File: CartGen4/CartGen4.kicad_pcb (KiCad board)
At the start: 4 copper layers, 52.8 x 60.9 mm, 81 parts, among them J1 MEM2080-00-128-00-A, J2 Conn_01x05_Male, J3 Conn_02x10_Odd_Even, SW1 EVQ-P7A01P, U1 TPS65266-1RHBR, U10 IS25WP080D-JNLE, U11 DS1391U-33+, U2 SN74LV1T34DCKR, U3 SIT8008BI-73-33E-33.333333G, U4 NXS0108BQX, U5 AS1C8M16PL-70BIN, U6 NXS0108BQX, U7 NXS0108BQX, U8 NXS0104BQX, U9 LFXP2-8E-5MN132C, Y1 FC-135R 32.7680KA-E5

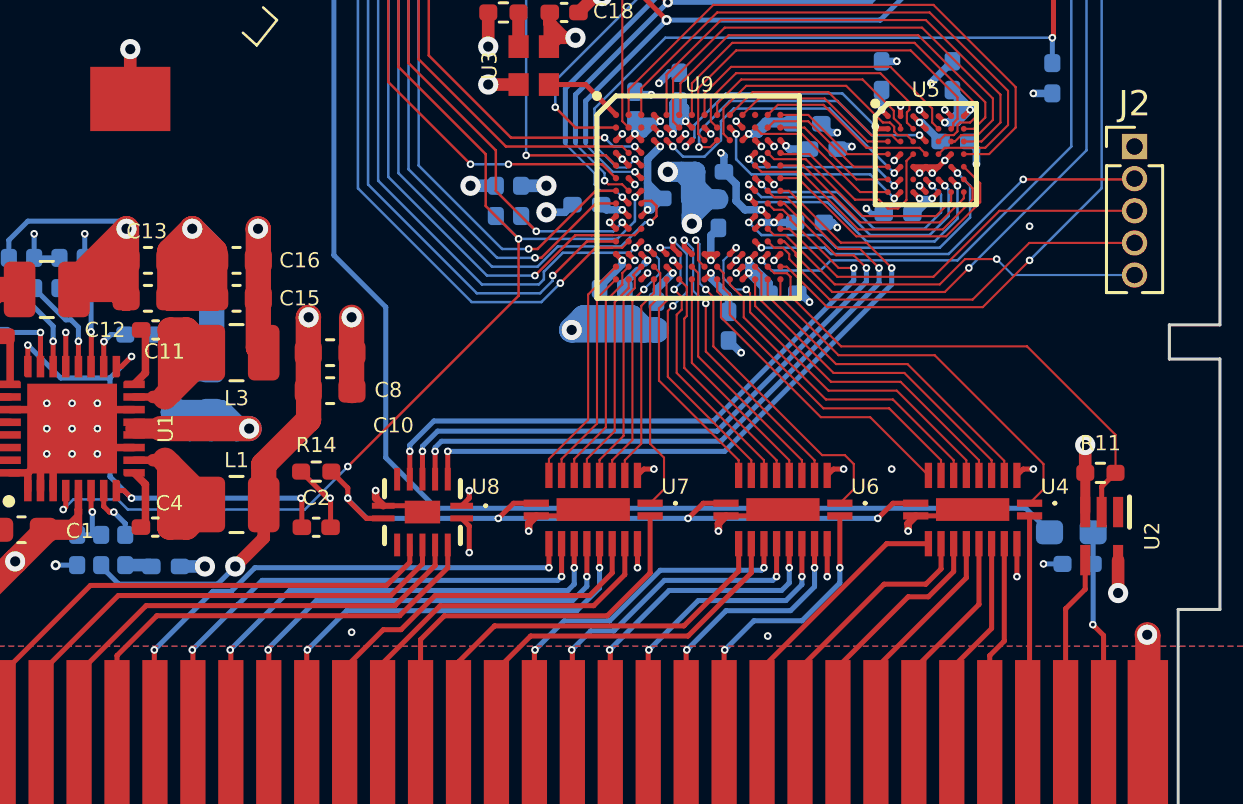
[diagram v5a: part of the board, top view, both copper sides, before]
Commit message: Added bypass capacitors to transceivers
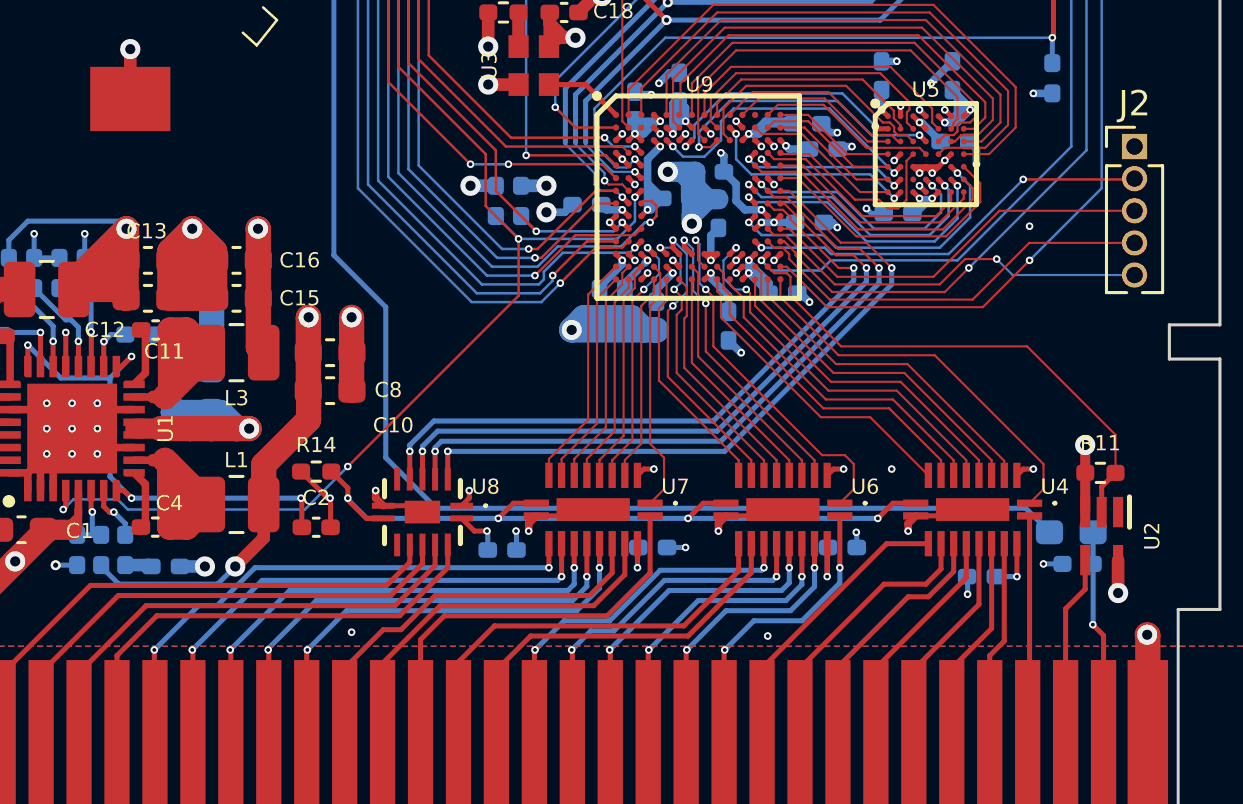
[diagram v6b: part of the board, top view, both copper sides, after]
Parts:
- added C41: 100n, Capacitor_SMD:C_0402_1005Metric_Pad0.74x0.62mm_HandSolder, B.Cu at (64.0, 87.6)
- added C42: 100n, Capacitor_SMD:C_0402_1005Metric_Pad0.74x0.62mm_HandSolder, B.Cu at (70.0, 87.5)
- added C43: 100n, Capacitor_SMD:C_0402_1005Metric_Pad0.74x0.62mm_HandSolder, B.Cu at (77.5, 87.5)
- added C44: 100n, Capacitor_SMD:C_0402_1005Metric_Pad0.74x0.62mm_HandSolder, B.Cu at (83.0, 88.7)
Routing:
- net +5V: track 33.1 -> 36.4 mm
- net GND: track 135.8 -> 138.5 mm, vias 83 -> 87
- net FPGA_USER5: track 42.9 -> 42.2 mm

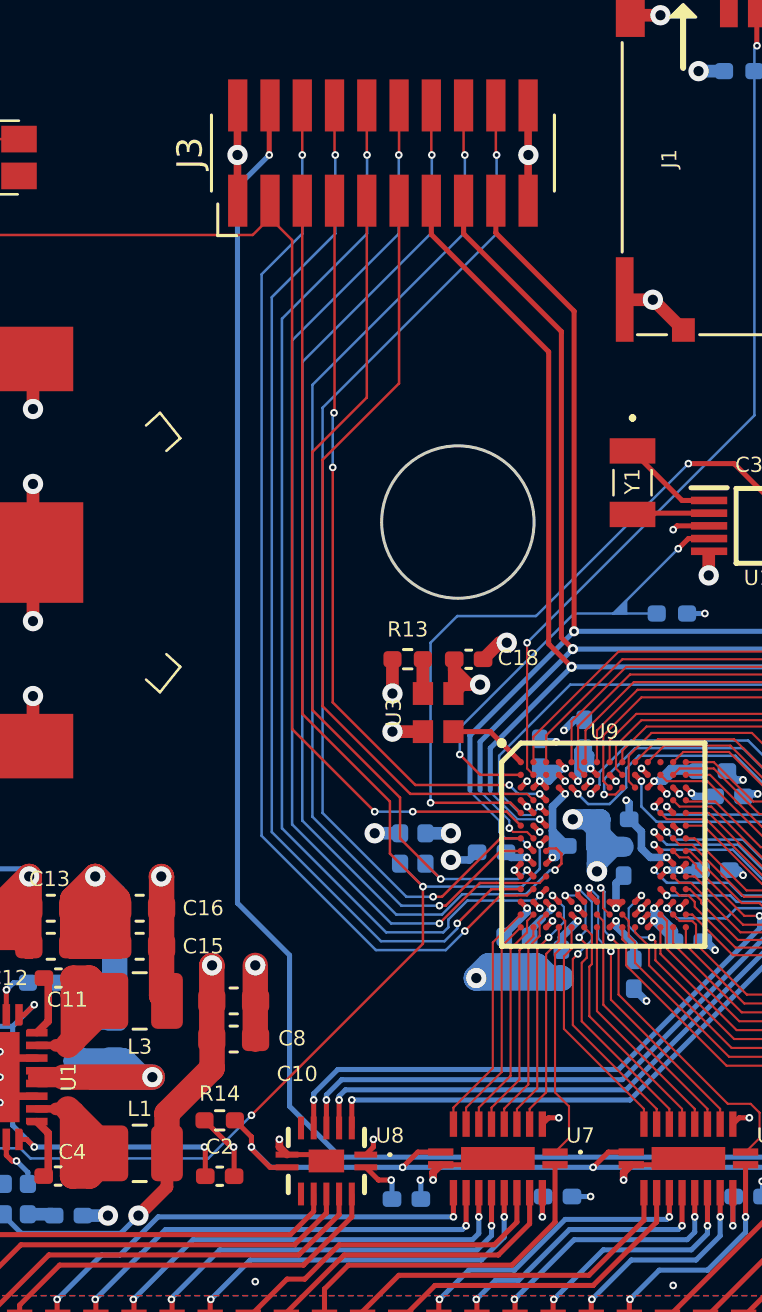
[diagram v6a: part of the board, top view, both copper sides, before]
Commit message: Routed almost forgotten GB_BUS_EN
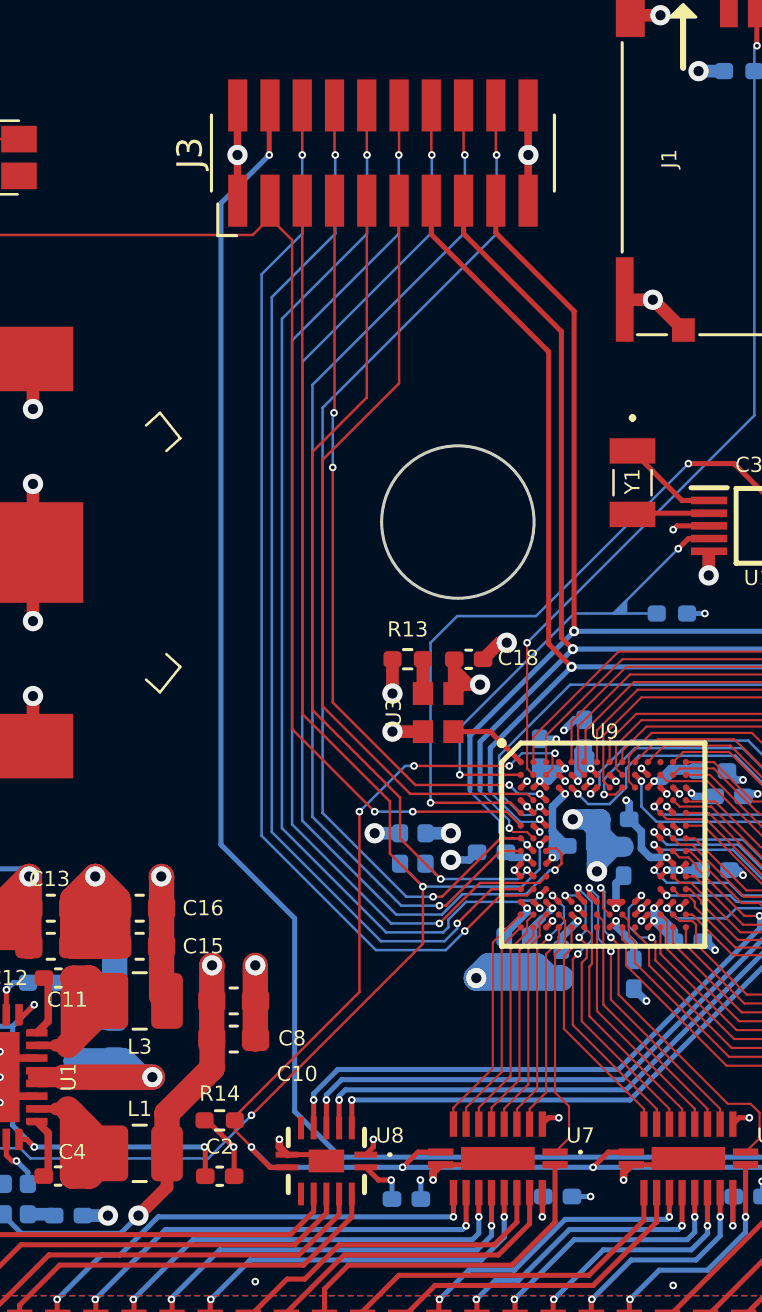
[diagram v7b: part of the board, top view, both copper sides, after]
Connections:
- U9 pad B3: unconnected-(U9-PadB3) -> GB_BUS_EN
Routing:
- net GB_BUS_EN: track 29.6 -> 53.4 mm, vias 4 -> 8
- net GB_AUDIO: track 68.2 -> 68.8 mm

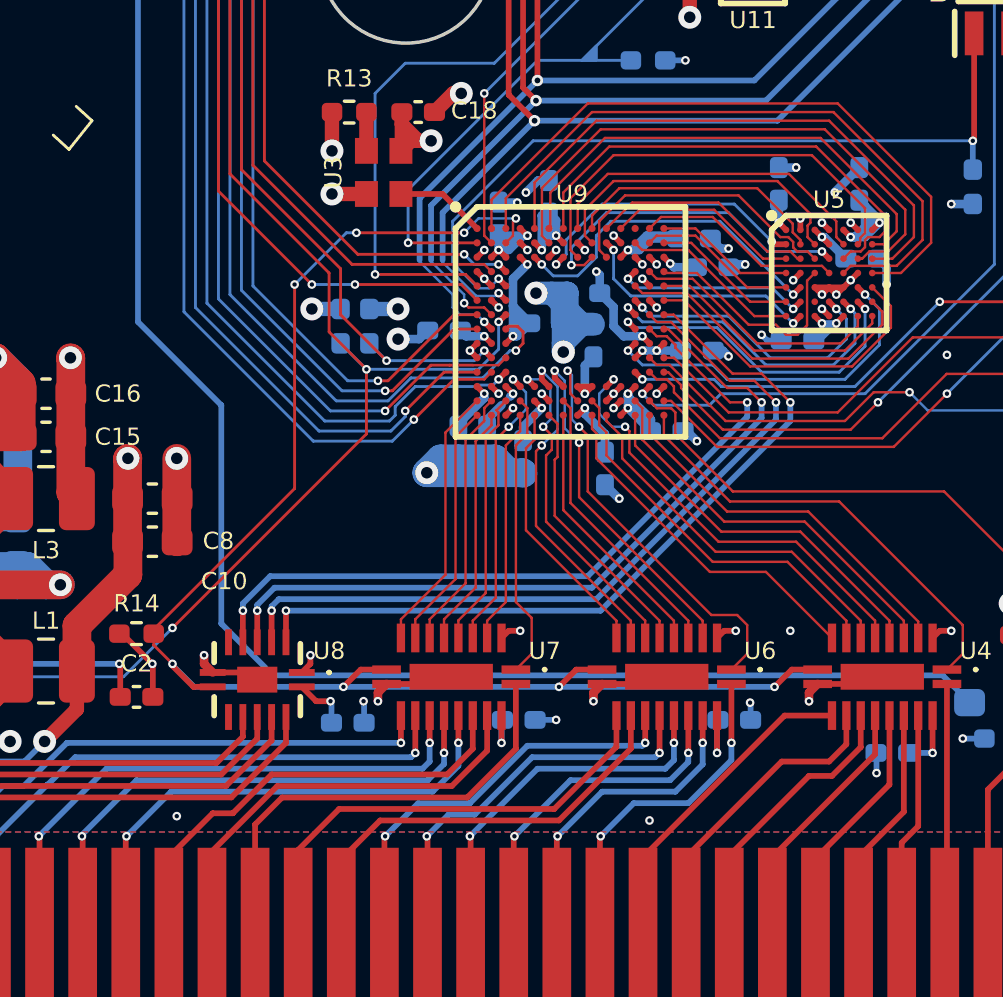
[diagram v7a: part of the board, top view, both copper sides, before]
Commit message: Added decoupling capacitor to lone 1V8 pin
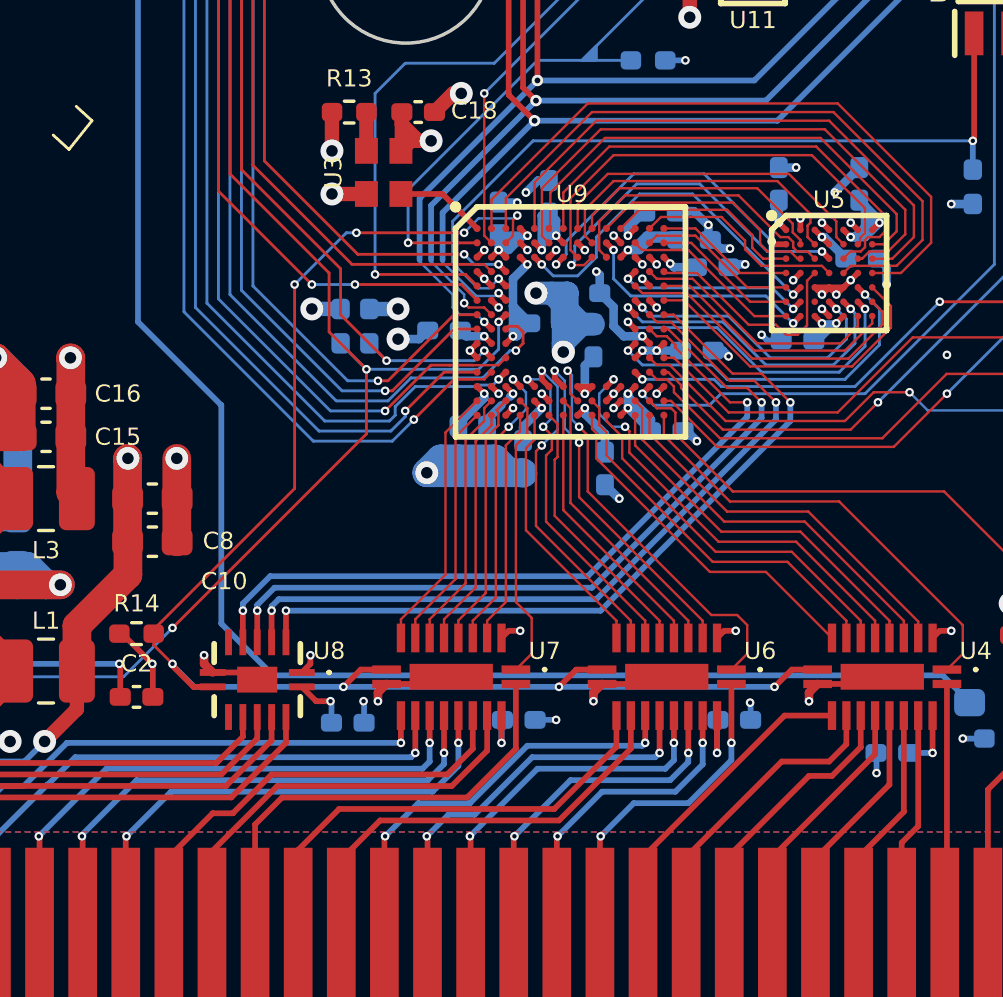
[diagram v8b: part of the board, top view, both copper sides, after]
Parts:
- added C45: 100n, Capacitor_SMD:C_0402_1005Metric_Pad0.74x0.62mm_HandSolder, B.Cu at (74.9, 69.8)
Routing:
- net GND: track 138.5 -> 140.3 mm, vias 87 -> 85
- net +1V8: track 40.0 -> 41.5 mm, vias 13 -> 14
- net +1V2: track 29.6 -> 30.8 mm
- net RAM_WAIT: track 10.1 -> 10.9 mm
- net RAM_OE#: track 11.6 -> 12.4 mm
- net RAM_ADV#: track 11.9 -> 12.7 mm
